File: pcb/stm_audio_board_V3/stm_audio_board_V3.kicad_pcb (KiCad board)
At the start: 4 copper layers, 66.1 x 71 mm, 147 parts, among them J1 Power conn, J2 STlink, J3 Audio_sig, J4 Conn_01x01_taptempo, J5 Conn_01x10_display, J6 Conn_01x03_pot_ext, J7 Conn_01x8_pots_internal, SW1 SW_SPST, U1 STM32H747IGTx, U2 OP275, U3 MP-K7805-500R3, U4 OP275, U5 MIC2920A-3.3WS-TR, U6 L7809, U9 MIC2920A-3.3WS-TR, Y2 X1E0000210132

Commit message: nothing
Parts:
- added RV1: R_Potentiometer, Potentiometer_THT:Potentiometer_Piher_T-16L_Single_Vertical_Hole, F.Cu at (196.7, 85.6)
- added RV2: R_Potentiometer, Potentiometer_THT:Potentiometer_Piher_T-16L_Single_Vertical_Hole, F.Cu at (189.4, 52.7)
- added RV3: R_Potentiometer, Potentiometer_THT:Potentiometer_Piher_T-16L_Single_Vertical_Hole, F.Cu at (209.4, 52.5)
- added RV4: R_Potentiometer, Potentiometer_THT:Potentiometer_Piher_T-16L_Single_Vertical_Hole, F.Cu at (239.4, 66.0)
- added RV5: R_Potentiometer, Potentiometer_THT:Potentiometer_Piher_T-16L_Single_Vertical_Hole, F.Cu at (240.2, 85.3)
- added RV6: R_Potentiometer, Potentiometer_THT:Potentiometer_Piher_T-16L_Single_Vertical_Hole, F.Cu at (219.3, 85.5)
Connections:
- U1 pad 113: +3.3V -> Net-(U1-VBAT)
- U1 pad 126: +3.3V -> Net-(U1-VBAT)
- U1 pad 13: +3.3V -> Net-(U1-VBAT)
- U1 pad 136: +3.3V -> Net-(U1-VBAT)
- U1 pad 152: +3.3V -> Net-(U1-VBAT)
- U1 pad 160: +3.3V -> Net-(U1-VBAT)
- U1 pad 176: +3.3V -> Net-(U1-VBAT)
- U1 pad 25: +3.3V -> Net-(U1-VBAT)
- U1 pad 44: +3.3V -> Net-(U1-VBAT)
- U1 pad 48: +3.3V -> Net-(U1-VBAT)
- U1 pad 65: +3.3V -> Net-(U1-VBAT)
- U1 pad 7: +3.3V -> Net-(U1-VBAT)
- U1 pad 71: +3.3V -> Net-(U1-VBAT)
- U1 pad 8: +3.3V -> Net-(U1-VBAT)
- U1 pad 84: +3.3V -> Net-(U1-VBAT)
- U1 pad 92: +3.3V -> Net-(U1-VBAT)
- U1 pad 99: +3.3V -> Net-(U1-VBAT)
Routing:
- net Net-(U1-VBAT): track 0.00 -> 3.92 mm
- net +3.3V: track 313.6 -> 309.7 mm
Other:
- board text added: "Date: 2024.02.09."
- board text removed: "Date: 2023.11.02."

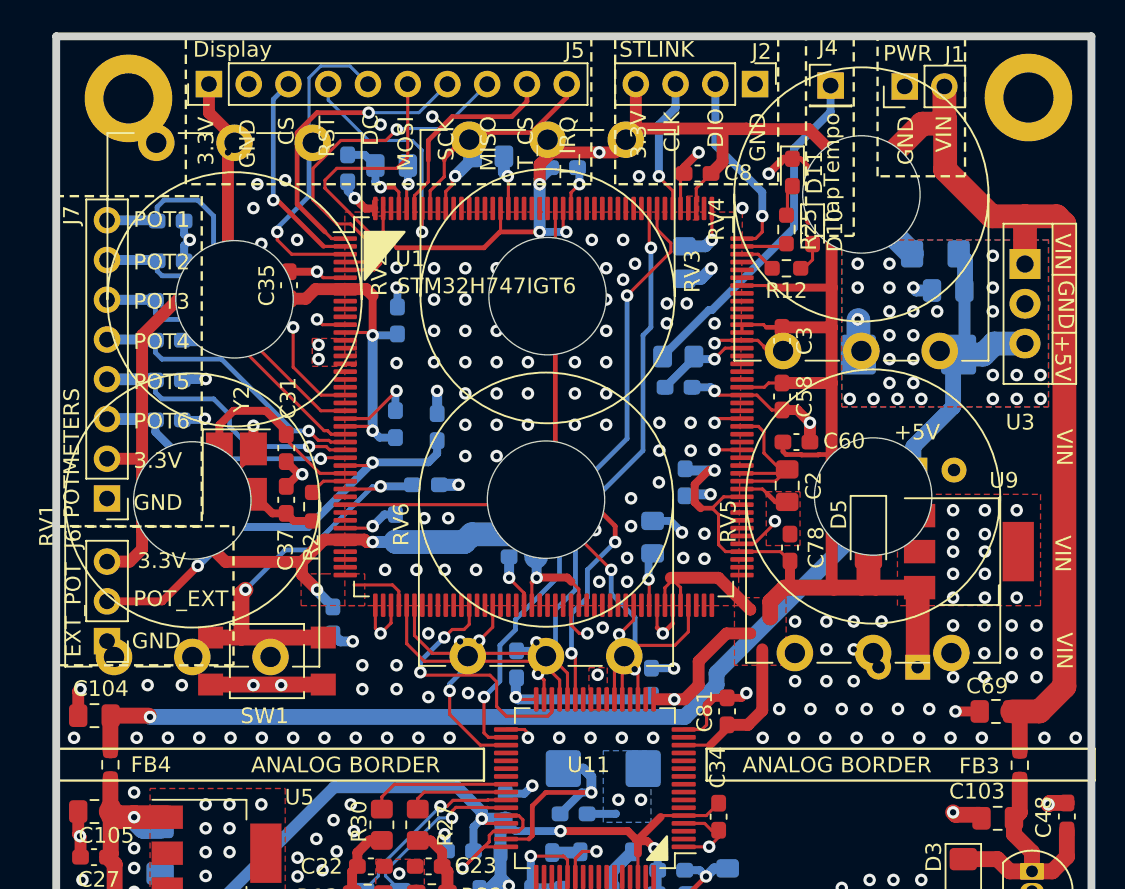
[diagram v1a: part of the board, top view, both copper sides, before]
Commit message: potmeter for V3 changed
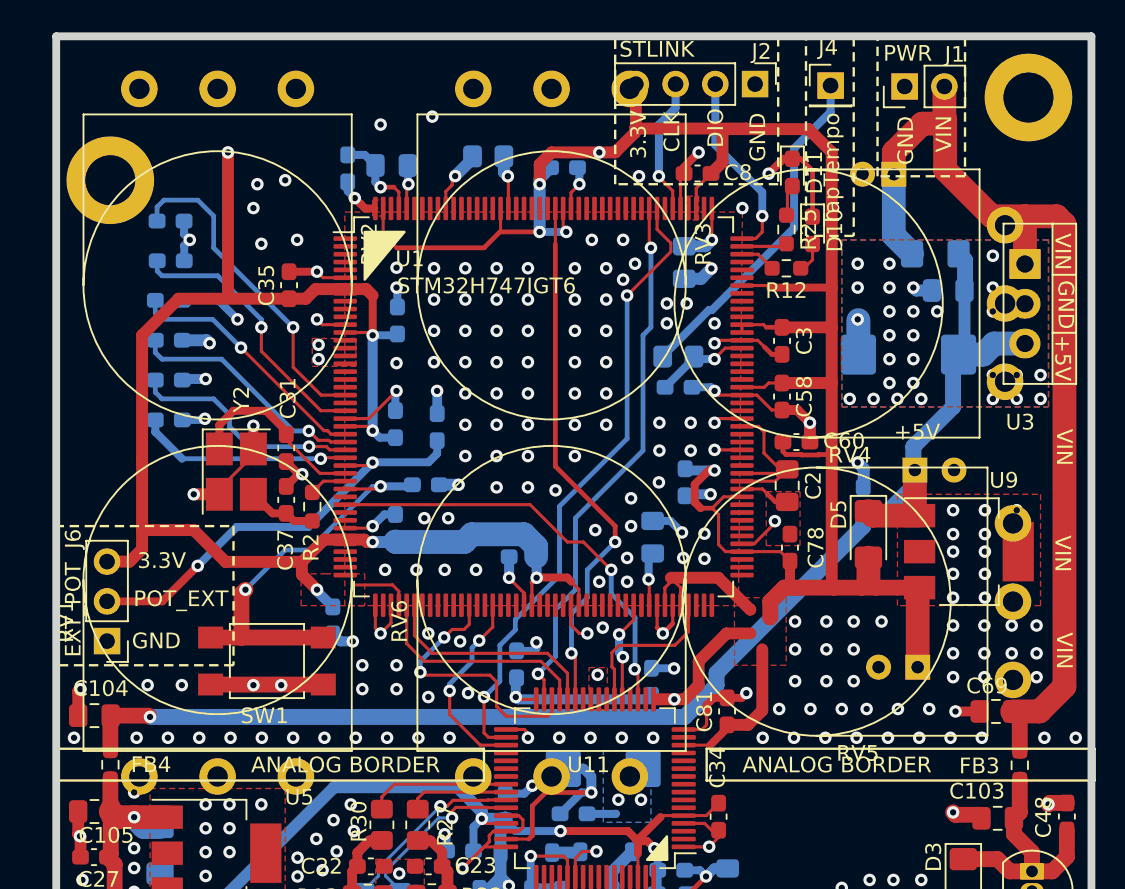
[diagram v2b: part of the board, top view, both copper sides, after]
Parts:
- removed J5: Conn_01x10_display, Connector_PinHeader_2.54mm:PinHeader_1x10_P2.54mm_Vertical
- removed J7: Conn_01x8_pots_internal, Connector_PinHeader_2.54mm:PinHeader_1x08_P2.54mm_Vertical
- RV1, RV2, RV3, RV4, RV5, RV6: footprint Potentiometer_THT:Potentiometer_Piher_T-16L_Single_Vertical_Hole -> Potentiometer_THT:Potentiometer_Omeg_PC16BU_Vertical
- moved RV5 9.17 mm to (244.1, 77.0), turned to 180 degrees
- moved RV4 9.06 mm to (243.6, 58.0), turned to 180 degrees
- moved RV1 7.81 mm to (198.3, 93.2)
- moved RV6 7.70 mm to (219.6, 93.2)
- moved H4 5.36 mm to (186.4, 55.1)
- moved RV2 3.61 mm to (188.3, 49.3)
- moved RV3 3.25 mm to (209.6, 49.3)
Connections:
- RV1 pad 1: unconnected-(RV1-Pad1) -> +3.3V
- RV1 pad 2: unconnected-(RV1-Pad2) -> POT1
- RV1 pad 3: unconnected-(RV1-Pad3) -> GND
- RV2 pad 1: unconnected-(RV2-Pad1) -> +3.3V
- RV2 pad 2: unconnected-(RV2-Pad2) -> POT2
- RV2 pad 3: unconnected-(RV2-Pad3) -> GND
- RV3 pad 1: unconnected-(RV3-Pad1) -> +3.3V
- RV3 pad 2: unconnected-(RV3-Pad2) -> POT3
- RV3 pad 3: unconnected-(RV3-Pad3) -> GND
- RV4 pad 1: unconnected-(RV4-Pad1) -> +3.3V
- RV4 pad 2: unconnected-(RV4-Pad2) -> POT4
- RV4 pad 3: unconnected-(RV4-Pad3) -> GND
- RV5 pad 1: unconnected-(RV5-Pad1) -> +3.3V
- RV5 pad 2: unconnected-(RV5-Pad2) -> POT5
- RV5 pad 3: unconnected-(RV5-Pad3) -> GND
- RV6 pad 1: unconnected-(RV6-Pad1) -> +3.3V
- RV6 pad 2: unconnected-(RV6-Pad2) -> POT6
- RV6 pad 3: unconnected-(RV6-Pad3) -> GND
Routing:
- net DISPLAY_MISO: track 22.5 -> 0.00 mm, vias 1 -> 0
- net DISPLAY_DC: track 20.5 -> 0.00 mm, vias 1 -> 0
- net DISPLAY_MOSI: track 19.8 -> 0.00 mm
- net DISPLAY_SCK: track 19.4 -> 0.00 mm, vias 1 -> 0
- net DISPLAY_RST: track 15.1 -> 0.00 mm, vias 1 -> 0
- net TOUCH_IRQ: track 13.9 -> 0.00 mm
- net DISPLAY_CS: track 13.6 -> 0.00 mm, vias 1 -> 0
- net TOUCH_CS: track 13.2 -> 0.00 mm
- net +3.3V: track 309.7 -> 302.5 mm
- net POT2: track 20.7 -> 17.5 mm
- net POT1: track 24.1 -> 20.9 mm
- net POT3: track 19.2 -> 16.1 mm
- net POT4: track 18.3 -> 15.3 mm
- net POT5: track 17.9 -> 14.9 mm
- net POT6: track 16.7 -> 13.6 mm
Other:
- board text removed: "CS"
- board text removed: "DC"
- board text removed: "Display"
- board text removed: "MISO"
- board text removed: "MOSI"
- board text removed: "POT1"
- board text removed: "POT2"
- board text removed: "POT3"
- board text removed: "POT4"
- board text removed: "POT5"
- board text removed: "POT6"
- board text removed: "POTMETERS"
- board text removed: "RST"
- board text removed: "SCK"
- board text removed: "T_CS"
- board text removed: "T_IRQ"

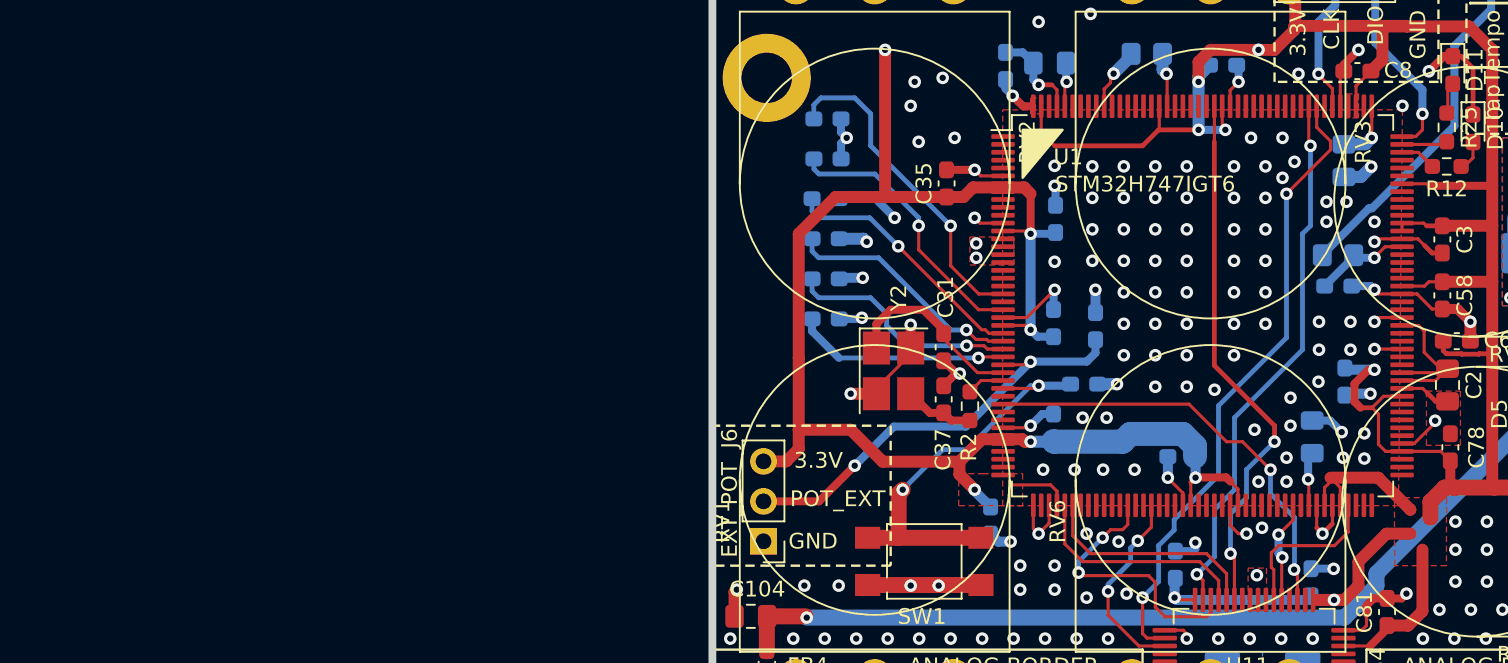
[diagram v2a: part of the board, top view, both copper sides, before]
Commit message: stm32h723 project for pinout added
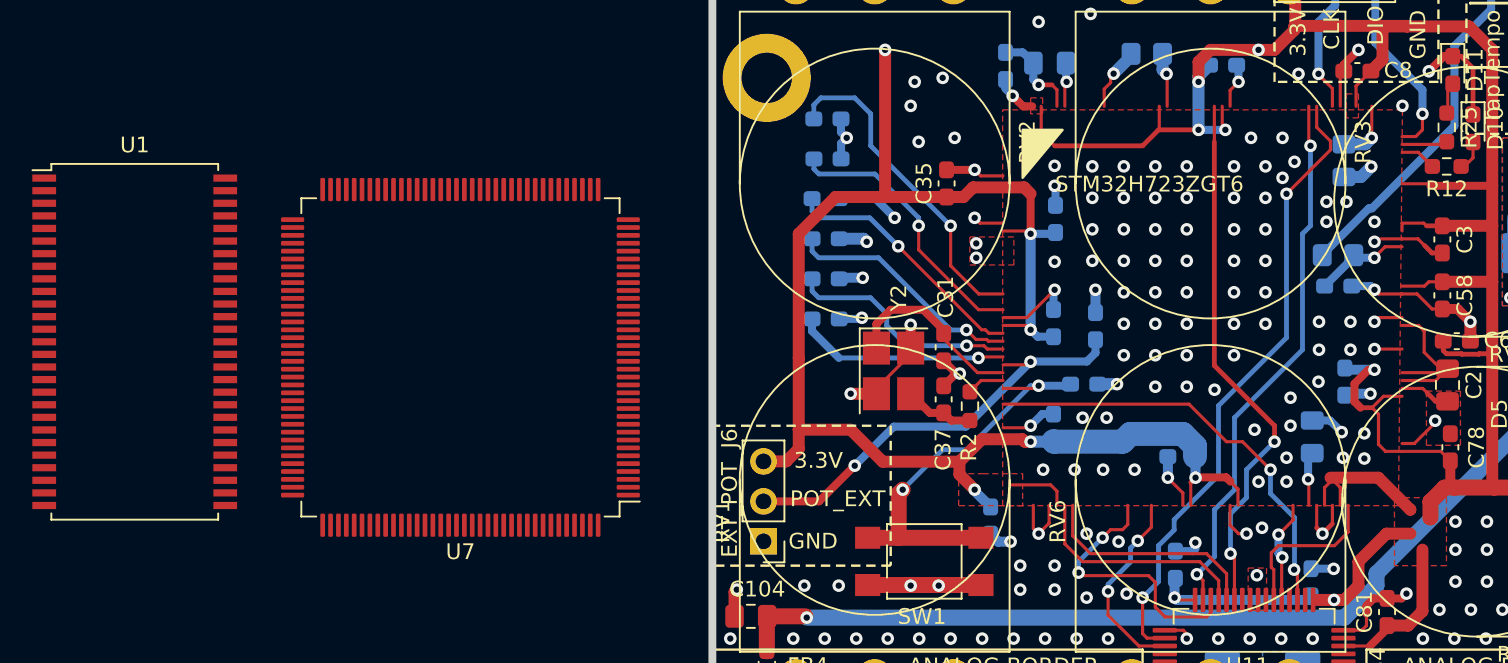
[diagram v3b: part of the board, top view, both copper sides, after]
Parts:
- added U7: STM32H723ZGTx, Package_QFP:LQFP-144_20x20mm_P0.5mm, F.Cu at (167.0, 72.9)
- U1: value STM32H747IGTx -> AS4C4M16SA; footprint Package_QFP:LQFP-176_24x24mm_P0.5mm -> Package_SO:TSOP-II-54_22.2x10.16mm_P0.8mm
- moved U1 67.9 mm to (146.3, 71.9)
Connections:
- C1 pad 1: Net-(C1-Pad1) -> unconnected-(C1-Pad1)
- C49 pad 1: Net-(C49-Pad1) -> unconnected-(C49-Pad1)
- C52 pad 1: Net-(C52-Pad1) -> unconnected-(C52-Pad1)
- R1 pad 1: Net-(U1-BOOT0) -> unconnected-(R1-Pad1)
- U1 pad 1: DISPLAY_SCK -> Net-(U1-VDD-Pad1)
- U1 pad 12: GND -> Net-(U1-VSSQ-Pad12)
- U1 pad 13: Net-(U1-VBAT) -> unconnected-(U1-DQ7-Pad13)
- U1 pad 14: GND -> Net-(U1-VDD-Pad1)
- U1 pad 15: GND -> unconnected-(U1-LDQM-Pad15)
- U1 pad 16: GND -> unconnected-(U1-~{WE}-Pad16)
- U1 pad 17: GND -> unconnected-(U1-~{CAS}-Pad17)
- U1 pad 2: DISPLAY_CS -> unconnected-(U1-DQ0-Pad2)
- U1 pad 21: POT1 -> unconnected-(U1-BA1-Pad21)
- U1 pad 23: POT2 -> unconnected-(U1-A0-Pad23)
- U1 pad 24: GND -> unconnected-(U1-A1-Pad24)
- U1 pad 25: Net-(U1-VBAT) -> unconnected-(U1-A2-Pad25)
- U1 pad 26: POT3 -> unconnected-(U1-A3-Pad26)
- U1 pad 27: POT4 -> Net-(U1-VDD-Pad1)
- U1 pad 28: POT5 -> Net-(U1-VSS-Pad28)
- U1 pad 29: POT6 -> unconnected-(U1-A4-Pad29)
- U1 pad 3: DISPLAY_DC -> Net-(U1-VDDQ-Pad3)
- U1 pad 30: POT_EXT -> unconnected-(U1-A5-Pad30)
- U1 pad 31: OSC0 -> unconnected-(U1-A6-Pad31)
- U1 pad 32: OSC1 -> unconnected-(U1-A7-Pad32)
- U1 pad 33: /MCU/NRST -> unconnected-(U1-A8-Pad33)
- U1 pad 35: AD1939_I2S2_SDO -> unconnected-(U1-A11-Pad35)
- U1 pad 38: GND -> unconnected-(U1-CLK-Pad38)
- U1 pad 39: +3.3V -> unconnected-(U1-UDQM-Pad39)
- U1 pad 4: DISPLAY_MISO -> unconnected-(U1-DQ1-Pad4)
- U1 pad 40: +3.3V -> unconnected-(U1-NC/RFU-Pad40)
- U1 pad 41: unconnected-(U1-PA0-Pad41) -> Net-(U1-VSS-Pad28)
- U1 pad 43: unconnected-(U1-PA2-Pad43) -> Net-(U1-VDDQ-Pad3)
- U1 pad 44: Net-(U1-VBAT) -> unconnected-(U1-DQ9-Pad44)
- U1 pad 45: GND -> unconnected-(U1-DQ10-Pad45)
- U1 pad 46: unconnected-(U1-PA3-Pad46) -> Net-(U1-VSSQ-Pad12)
- U1 pad 47: GND -> unconnected-(U1-DQ11-Pad47)
- U1 pad 48: Net-(U1-VBAT) -> unconnected-(U1-DQ12-Pad48)
- U1 pad 49: AD1939_I2S1_WS -> Net-(U1-VDDQ-Pad3)
- U1 pad 5: DISPLAY_MOSI -> unconnected-(U1-DQ2-Pad5)
- U1 pad 50: AD1939_I2S1_CK -> unconnected-(U1-DQ13-Pad50)
- U1 pad 52: unconnected-(U1-PA7-Pad52) -> Net-(U1-VSSQ-Pad12)
- U1 pad 54: unconnected-(U1-PC5-Pad54) -> Net-(U1-VSS-Pad28)
- U1 pad 6: GND -> Net-(U1-VSSQ-Pad12)
- U1 pad 7: Net-(U1-VBAT) -> unconnected-(U1-DQ3-Pad7)
- U1 pad 8: Net-(U1-VBAT) -> unconnected-(U1-DQ4-Pad8)
- U1 pad 9: unconnected-(U1-PC13-Pad9) -> Net-(U1-VDDQ-Pad3)
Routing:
- net unconnected-(R1-Pad1): track 0.00 -> 4.04 mm, vias 0 -> 1
- net Net-(U1-BOOT0): track 4.04 -> 0.00 mm, vias 1 -> 0
- net unconnected-(C49-Pad1): track 0.00 -> 3.94 mm, vias 0 -> 1
- net Net-(C49-Pad1): track 3.94 -> 0.00 mm, vias 1 -> 0
- net Net-(U1-VBAT): track 3.92 -> 0.00 mm
- net (no net): track 0.00 -> 3.92 mm
- net unconnected-(C1-Pad1): track 0.00 -> 3.44 mm, vias 0 -> 1
- net Net-(C1-Pad1): track 3.44 -> 0.00 mm, vias 1 -> 0
- net unconnected-(C52-Pad1): track 0.00 -> 2.86 mm, vias 0 -> 1
- net Net-(C52-Pad1): track 2.86 -> 0.00 mm, vias 1 -> 0
- net unconnected-(U7-PE6-Pad5): track 0.00 -> 1.94 mm, vias 0 -> 1
- net GND: track 200.3 -> 198.4 mm, vias 314 -> 312
- net unconnected-(U7-PB13-Pad74): vias 0 -> 1
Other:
- board text added: "STM32H723ZGT6"
